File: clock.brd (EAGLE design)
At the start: 69 x 66 mm, 40 parts, among them IC3 7805TV, J1 J10MM, J2 J10MM, J3 J7MM, J4 J7MM, J5 J5MM, J6 J30MM, Q1 BC547, Q2 BC547, U1 ATTINY45-P

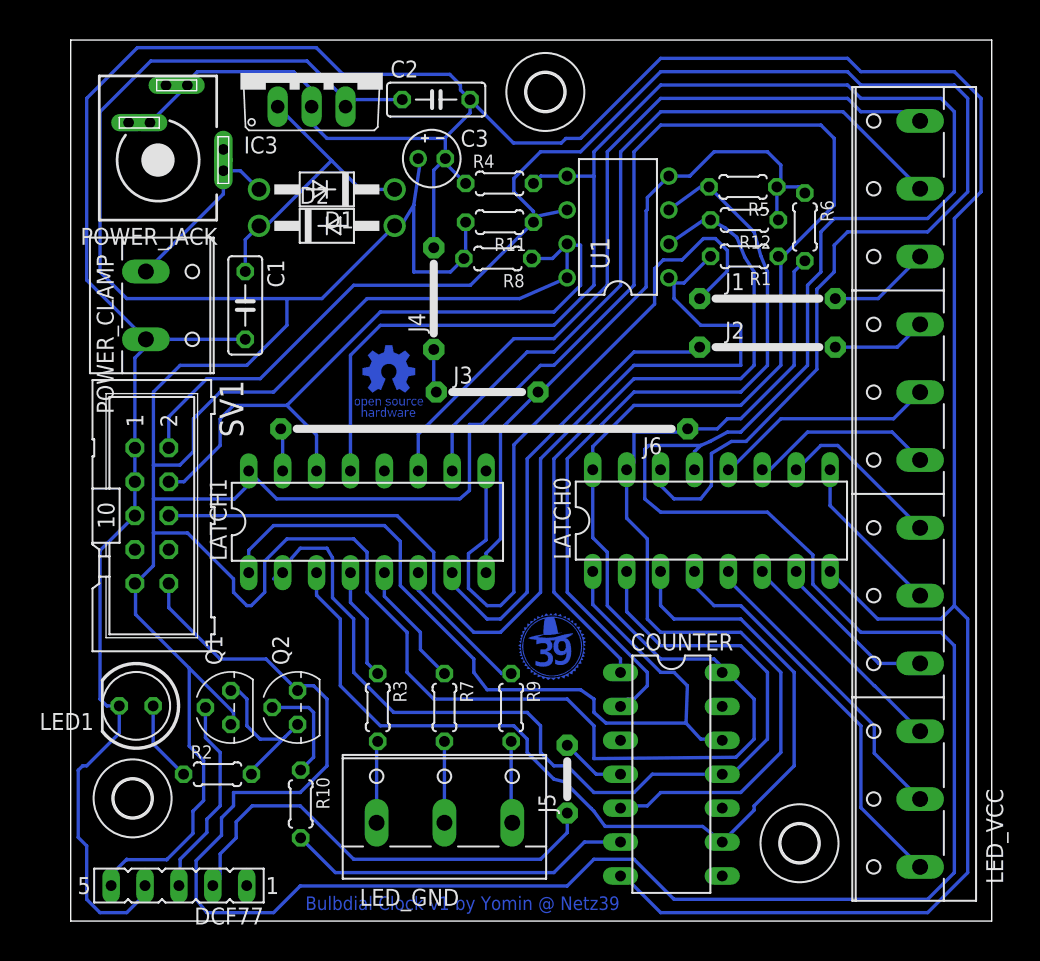
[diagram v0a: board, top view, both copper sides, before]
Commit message: change powerjack to horizontal, fix DRC errors, mirror logos and text, add gnd plane, set wire width to 12mil
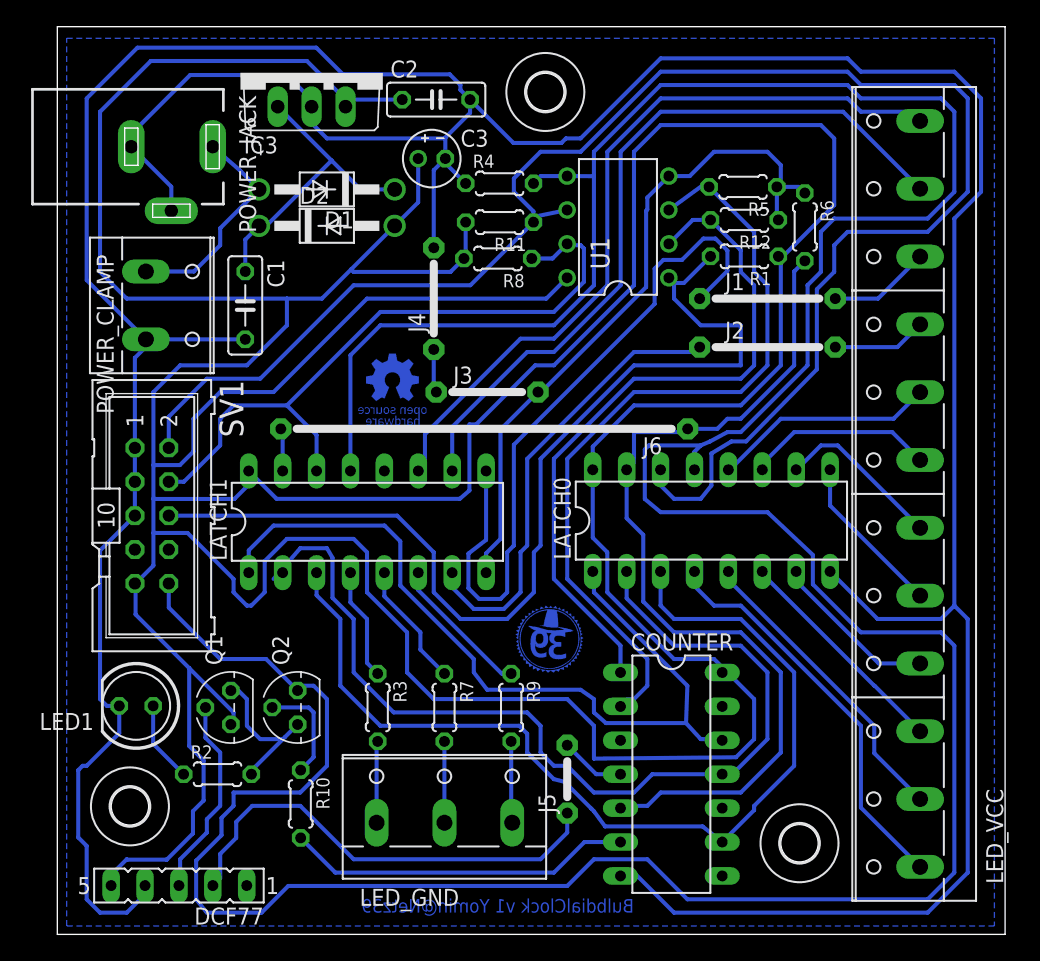
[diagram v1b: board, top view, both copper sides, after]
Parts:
- POWER_JACK: value KLDVX-0202-B -> DCJ0202; device con-kycon:KLDVX-0202-B -> con-jack:DCJ0202
- moved POWER_JACK 1.41 mm to (6.34, 73.4), turned to 270 degrees
- moved U$2 0.63 mm to (3.24, 24.0)
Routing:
- net GND: track 351.4 -> 360.8 mm
- net +12V: track 13.2 -> 16.5 mm
- net +5V: track 388.5 -> 385.3 mm
- net N$23: track 76.5 -> 75.4 mm
- net N$31: track 34.8 -> 34.0 mm
- net N$30: track 53.6 -> 52.9 mm
- net N$24: track 62.6 -> 62.0 mm
- net N$28: track 73.1 -> 72.5 mm
- net N$22: track 68.5 -> 67.9 mm
- added copper zone on layer 16, net GND
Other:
- board size 69 x 66 mm -> 71 x 68 mm
- board text added: "BulbdialClock v1 Yomin@Netz39"
- board text removed: "Bulbdial Clock v1 by Yomin @ Netz39"

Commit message: fix ERC errors of schematic, add missing VCC/VSS pins of ICs, replace jumpers with vias
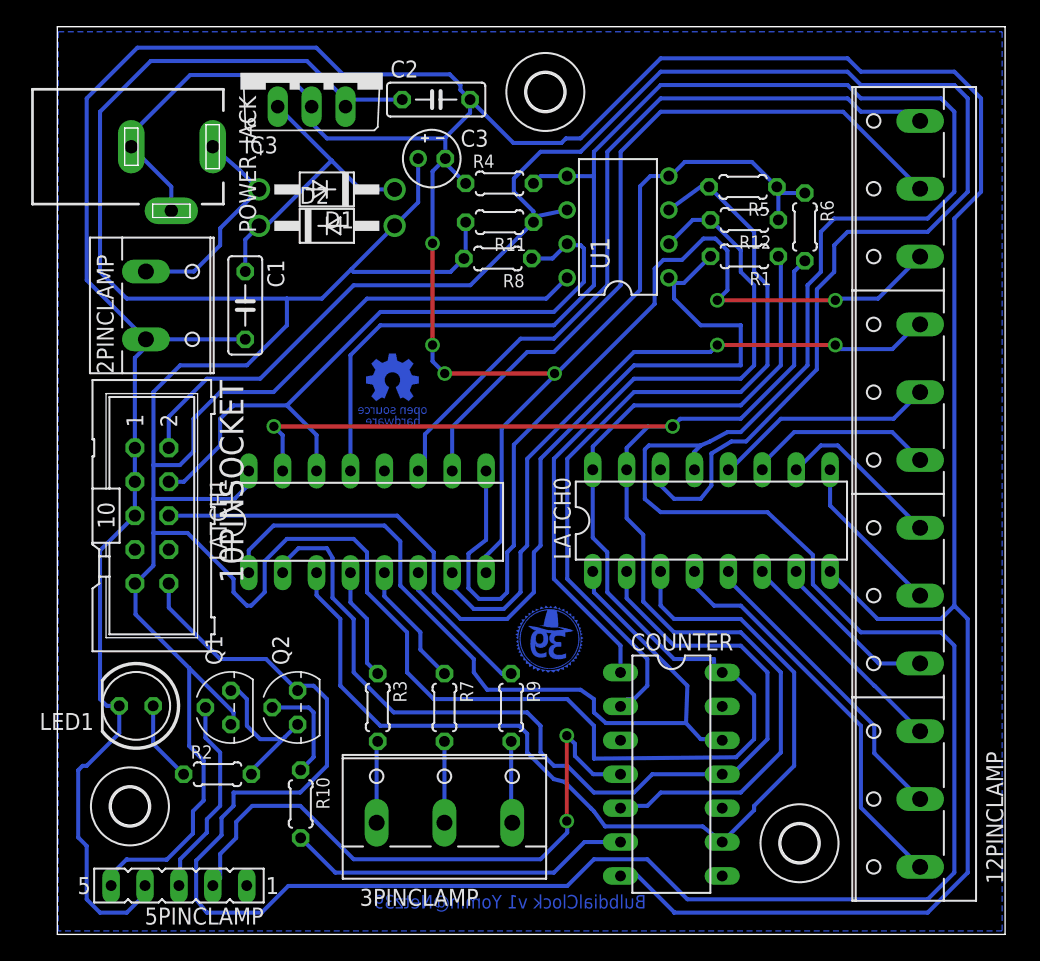
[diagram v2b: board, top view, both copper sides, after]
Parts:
- removed J1, J2: J10MM, jumper:10
- removed J3, J4: J7MM, jumper:07
- removed J5: J5MM, jumper:05
- removed J6: J30MM, jumper:30
- 10PINSOCKET: value (none) -> ISP
- 12PINCLAMP: value (none) -> LED VCC
- 2PINCLAMP: value (none) -> POWER CLAMP
- 3PINCLAMP: value (none) -> LED GND
- 5PINCLAMP: value (none) -> DCF77
- LED1: value (none) -> DCF Status
- renumbered DCF77 to 5PINCLAMP, LED_GND to 3PINCLAMP, LED_VCC to 12PINCLAMP, POWER_CLAMP to 2PINCLAMP, SV1 to 10PINSOCKET
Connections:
- removed net N$12: 12PINCLAMP.10, J1.2
- removed net N$29: LATCH1.2
- removed net N$31: J2.1, LATCH1.7
- removed net N$32: 5PINCLAMP.2, J5.1
- removed net N$33: J6.2, LATCH1.15
- removed net VDD: COUNTER.14
- removed net VSS: COUNTER.7
- net +5V: now also COUNTER.14
- net DCF_PON: now also 5PINCLAMP.2; no longer J5.2
- net GND: now also COUNTER.7; no longer J3.1, J3.2, J4.1, J4.2
- net N$11: now also LATCH1.7; no longer J2.2
- net N$22: now also LATCH1.15; no longer J6.1
- net N$28: now also LATCH1.2
- net N$30: now also 12PINCLAMP.10; no longer J1.1
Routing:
- net +5V: track 385.3 -> 309.3 mm
- net N$11: track 7.16 -> 51.5 mm, vias 0 -> 2
- net DCF_PON: track 4.89 -> 46.3 mm, vias 0 -> 2
- net N$32: track 34.7 -> 0.00 mm
- net N$31: track 34.0 -> 0.00 mm
- net N$22: track 67.9 -> 101.0 mm, vias 0 -> 2
- net N$30: track 52.9 -> 69.0 mm, vias 0 -> 2
- net GND: track 360.8 -> 373.4 mm, vias 0 -> 4
- net N$12: track 7.66 -> 0.00 mm
- net N$33: track 3.21 -> 0.00 mm
- net N$28: track 72.5 -> 71.9 mm

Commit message: rotate isp 180°, connect 4th gnd pin, move logo/text to doc layer
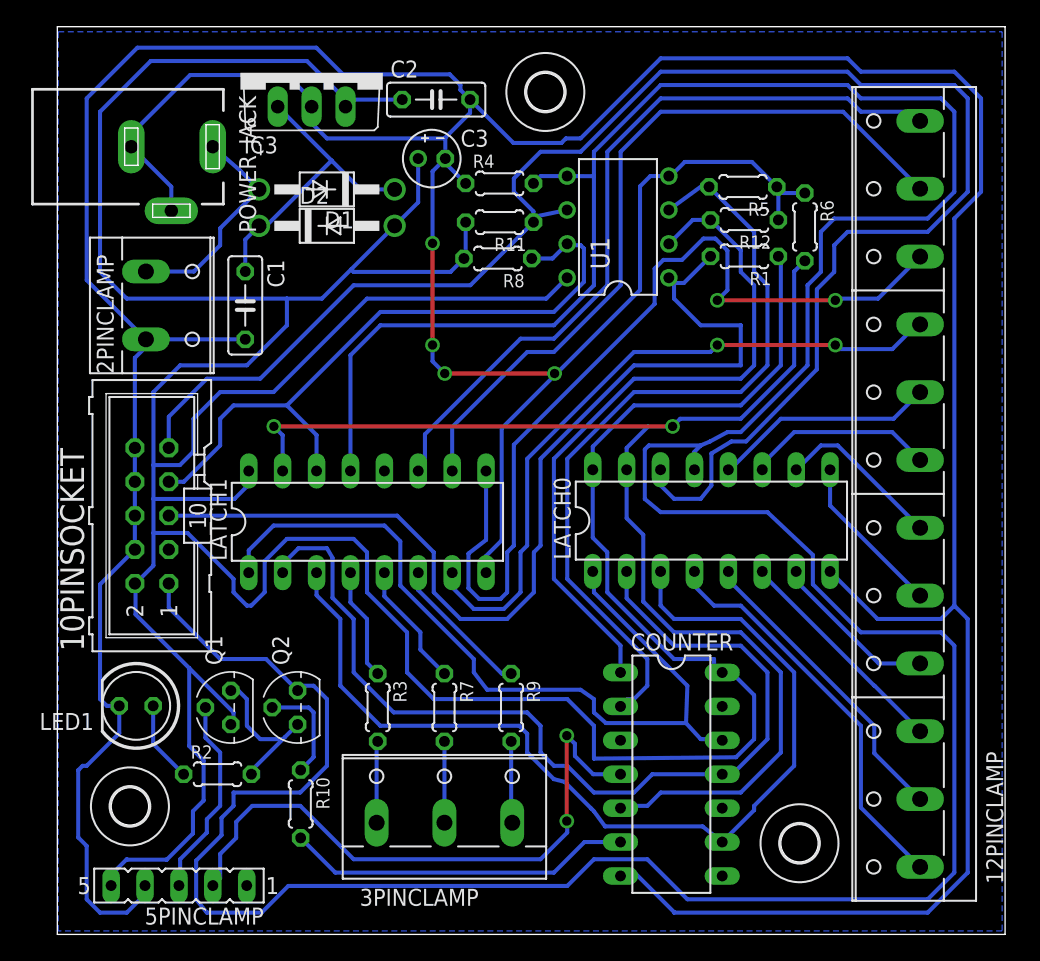
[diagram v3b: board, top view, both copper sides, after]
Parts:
- turned 10PINSOCKET to 90 degrees
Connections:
- net +5V: now also 10PINSOCKET.2; no longer 10PINSOCKET.9
- net DATA: now also 10PINSOCKET.1; no longer 10PINSOCKET.10
- net GND: now also 10PINSOCKET.10, 10PINSOCKET.4, 10PINSOCKET.6, 10PINSOCKET.8; no longer 10PINSOCKET.1, 10PINSOCKET.3, 10PINSOCKET.5
- net LATCH0: now also 10PINSOCKET.7; no longer 10PINSOCKET.4
- net LATCH1: now also 10PINSOCKET.9; no longer 10PINSOCKET.2
- net N$23: now also 10PINSOCKET.5; no longer 10PINSOCKET.6
